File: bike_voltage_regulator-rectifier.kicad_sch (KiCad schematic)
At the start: 25 parts, among them U1 GBU1510_C22447862, U2 IRFB4110PBF, U3 MBR2045CT_C173461, U4 LM2903DRG4, U5 TL431_C181103, U6 MMBT3904, U7 MMBT3906LT1G, U8 436500400

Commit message: first prototype
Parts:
- U8: now not fitted; now left out of the parts list
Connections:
- net AC1: now also U8.4; no longer U8.1
- net AC2: now also U8.3; no longer U8.2
- net GND: now also U8.2; no longer U8.4
- net VOUT: now also U8.1; no longer U8.3
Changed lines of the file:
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@@
 	(wire
 		(pts
+			(xy 100.33 139.7) (xy 104.14 139.7)
+		)
+		(stroke
+			(width 0)
+			(type default)
+		)
+	)
+	(wire
+		(pts
 			(xy 151.13 114.3) (xy 151.13 144.78)
 		)
@@
 	(wire
 		(pts
-			(xy 100.33 144.78) (xy 102.87 144.78)
-		)
-		(stroke
-			(width 0)
-			(type default)
-		)
-	)
-	(wire
-		(pts
 			(xy 142.24 153.67) (xy 151.13 153.67)
 		)
@@
 	(wire
 		(pts
-			(xy 102.87 144.78) (xy 102.87 147.32)
-		)
-		(stroke
-			(width 0)
-			(type default)
-		)
-	)
-	(wire
-		(pts
 			(xy 168.91 119.38) (xy 171.45 119.38)
 		)
@@
 	(global_label "AC1"
 		(shape input)
-		(at 100.33 137.16 0)
+		(at 100.33 144.78 0)
 		(fields_autoplaced yes)
 		(effects
@@
 		)
 		(property "Intersheetrefs" "${INTERSHEET_REFS}"
-			(at 106.8833 137.16 0)
+			(at 106.8833 144.78 0)
 			(hide yes)
 			(show_name no)
@@
 	(global_label "AC2"
 		(shape input)
-		(at 100.33 139.7 0)
+		(at 100.33 142.24 0)
 		(fields_autoplaced yes)
 		(effects
@@
 		)
 		(property "Intersheetrefs" "${INTERSHEET_REFS}"
-			(at 106.8833 139.7 0)
+			(at 106.8833 142.24 0)
 			(hide yes)
 			(show_name no)
@@
 	(global_label "VOUT"
 		(shape input)
-		(at 100.33 142.24 0)
+		(at 100.33 137.16 0)
 		(fields_autoplaced yes)
 		(effects
@@
 		)
 		(property "Intersheetrefs" "${INTERSHEET_REFS}"
-			(at 108.0324 142.24 0)
+			(at 108.0324 137.16 0)
 			(hide yes)
 			(show_name no)
@@
 	(symbol
 		(lib_id "power:GND")
-		(at 102.87 147.32 0)
+		(at 104.14 139.7 90)
 		(unit 1)
 		(body_style 1)
@@
 		(fields_autoplaced yes)
 		(property "Reference" "#PWR017"
-			(at 102.87 153.67 0)
+			(at 110.49 139.7 0)
 			(hide yes)
 			(show_name no)
@@
 		)
 		(property "Value" "GND"
-			(at 102.87 152.4 0)
+			(at 107.95 139.6999 90)
 			(show_name no)
 			(do_not_autoplace no)
@@
 					(size 1.27 1.27)
 				)
+				(justify right)
 			)
 		)
 		(property "Footprint" ""
-			(at 102.87 147.32 0)
+			(at 104.14 139.7 0)
 			(hide yes)
 			(show_name no)
@@
 		)
 		(property "Datasheet" ""
-			(at 102.87 147.32 0)
+			(at 104.14 139.7 0)
 			(hide yes)
 			(show_name no)
@@
 		)
 		(property "Description" "Power symbol creates a global label with name \"GND\" , ground"
-			(at 102.87 147.32 0)
+			(at 104.14 139.7 0)
 			(hide yes)
 			(show_name no)
@@
 		(body_style 1)
 		(exclude_from_sim no)
-		(in_bom yes)
+		(in_bom no)
 		(on_board yes)
 		(in_pos_files yes)
-		(dnp no)
+		(dnp yes)
 		(fields_autoplaced yes)
 		(property "Reference" "U8"

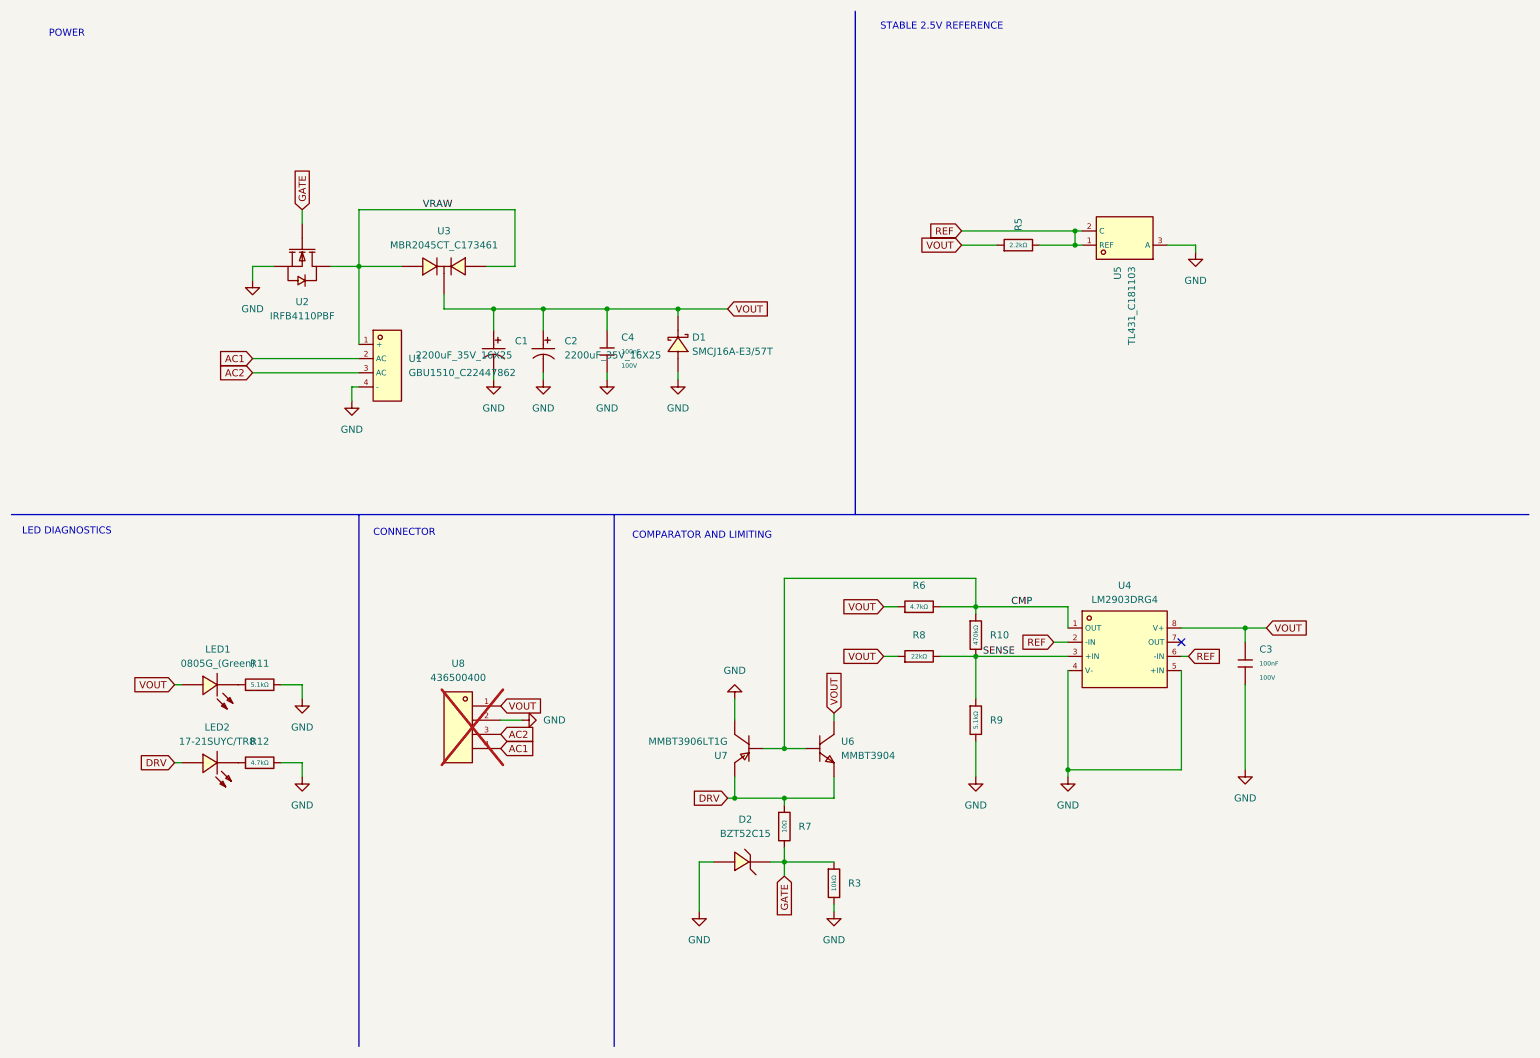
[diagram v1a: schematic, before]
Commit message: Changed rectification architecture
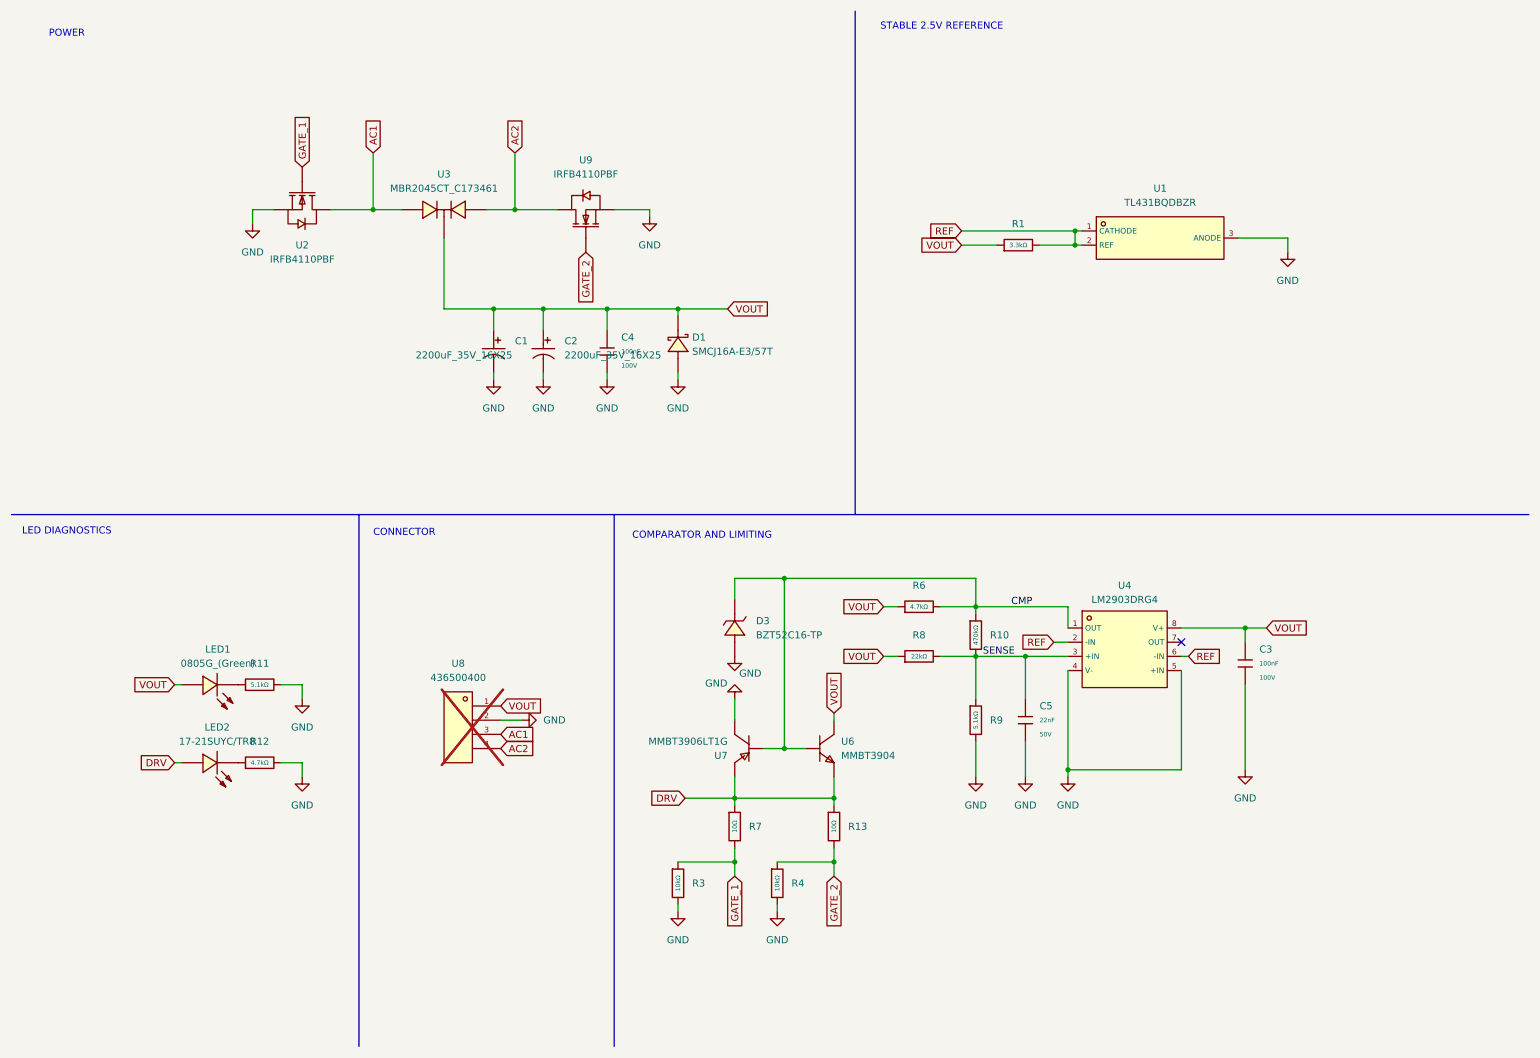
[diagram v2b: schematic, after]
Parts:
- removed D2: BZT52C15, regulator_library:SOD-123_L2.7-W1.6-LS3.7-RD, symbol regulator_library:BZT52C15
- removed R5: 2.2kΩ, PCM_JLCPCB:R_0805, symbol PCM_JLCPCB-Resistors:0805,2.2kΩ
- removed U1: GBU1510_C22447862, regulator_library:GBU_4P-L22.0-W3.5-P5.08_GBU808, symbol regulator_library:GBU1510_C22447862
- removed U5: TL431_C181103, regulator_library:SOT-23-3_L3.0-W1.7-P0.95-LS2.9-BR, symbol regulator_library:TL431_C181103
- added C5: 22nF, PCM_JLCPCB:C_0805, symbol PCM_JLCPCB-Capacitors:0805,22nF
- added D3: BZT52C16-TP, regulator_library:SOD-123_L2.8-W1.8-LS3.7-RD, symbol regulator_library:BZT52C16-TP
- added R1: 3.3kΩ, PCM_JLCPCB:R_0805, symbol PCM_JLCPCB-Resistors:0805,3.3kΩ
- added R13: 10Ω, PCM_JLCPCB:R_0805, symbol PCM_JLCPCB-Resistors:0805,10Ω
- added R4: 10kΩ, PCM_JLCPCB:R_0805, symbol PCM_JLCPCB-Resistors:0805,10kΩ
- added U1: TL431BQDBZR, regulator_library:SOT-23-3_L2.9-W1.6-P1.90-LS2.8-BR, symbol regulator_library:TL431BQDBZR
- added U9: IRFB4110PBF, regulator_library:TO-220-3_L10.0-W4.5-P2.54-L, symbol regulator_library:IRFB4110PBF
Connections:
- net AC1: now also U2.2 (D), U3.1 (A), U8.3; no longer U8.4
- net AC2: now also U3.3 (A), U8.4, U9.2 (D); no longer U8.3
- net CMP: now also D3.1 (C)
- net DRV: now also R13.1
- net GND: now also C5.2, D3.2 (A), R4.2, U1.3 (ANODE), U9.3 (S)
- net REF: now also R1.2, U1.1 (CATHODE), U1.2 (REF)
- net SENSE: now also C5.1
- net VOUT: now also R1.1
- net GATE renamed GATE_1
- removed net VRAW: U2.2 (D), U3.1 (A), U3.3 (A)
- new net GATE_2: R13.2, R4.1, U9.1 (G)
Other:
- moved on the sheet: R3, R7, U2, U3
